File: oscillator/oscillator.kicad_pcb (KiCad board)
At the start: 2 copper layers, 80.5 x 147.8 mm, 37 parts, among them J1 Output, J2 Output, J3 Triangle Output, J4 Saw Output, J5 Pulse Output, J6 Frequency CV Input, J7 PWM CV Input, SW1 LFO Switch, U1 AS3340-custom, U2 TL074

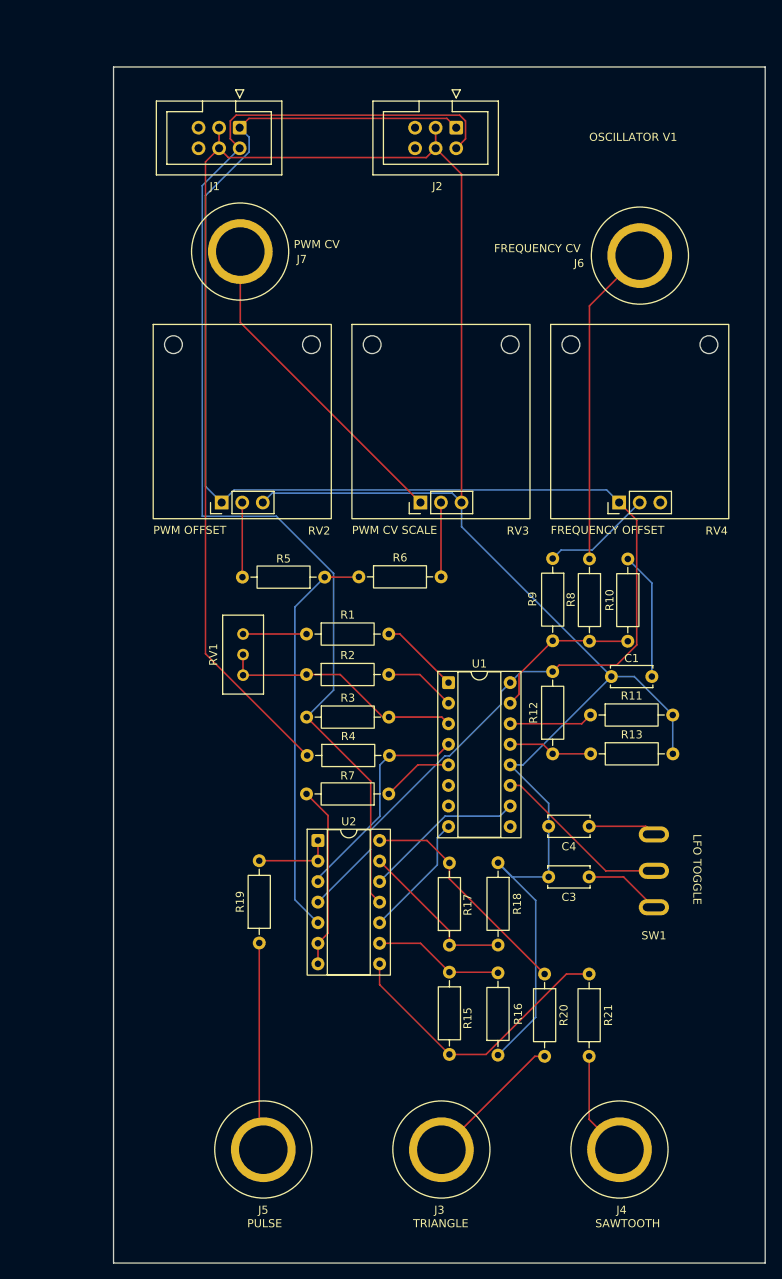
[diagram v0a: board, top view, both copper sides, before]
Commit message: Redesign oscillator
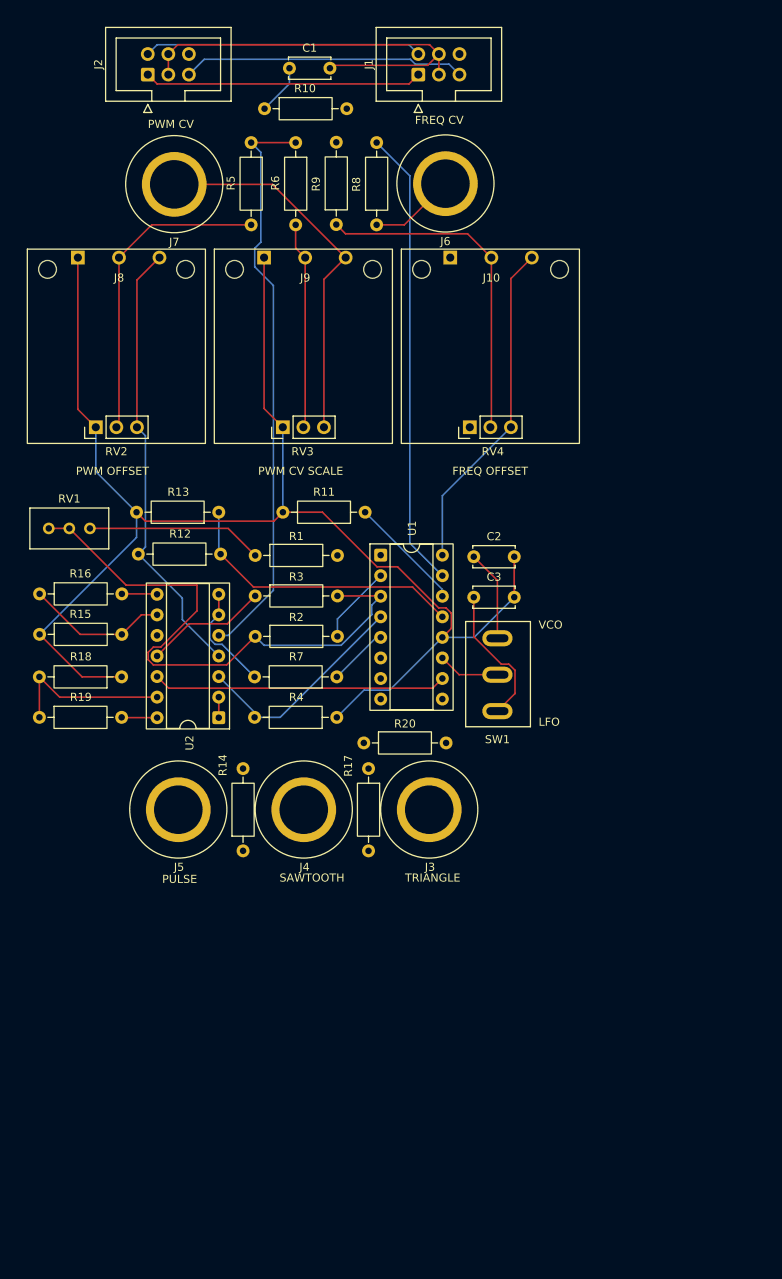
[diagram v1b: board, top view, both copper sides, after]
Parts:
- removed C4: 470nF, Capacitor_THT:C_Disc_D5.0mm_W2.5mm_P5.00mm
- removed R21: 1K, Resistor_THT:R_Axial_DIN0207_L6.3mm_D2.5mm_P10.16mm_Horizontal
- added C2: 4.7nF, Capacitor_THT:C_Disc_D5.0mm_W2.5mm_P5.00mm, F.Cu at (106.0, 92.8)
- added J10: Conn_01x03_Socket, modular2:pot, F.Cu at (108.2, 58.8)
- added J8: Conn_01x03_Socket, modular2:pot, F.Cu at (62.2, 58.8)
- added J9: Conn_01x03_Socket, modular2:pot, F.Cu at (85.2, 58.8)
- added R14: 1K, Resistor_THT:R_Axial_DIN0207_L6.3mm_D2.5mm_P10.16mm_Horizontal, F.Cu at (77.5, 129.1)
- C3: value 4.7nF -> 470nF
- R15: value 24K -> 100K
- R16: value 100K -> 24K
- R17: value 20K -> 1K
- R19: value 1K -> 20K
- moved C1 87.5 mm to (83.2, 32.4), turned to 0 degrees
- moved R16 80.3 mm to (52.4, 97.3), turned to 0 degrees
- moved R10 71.5 mm to (80.2, 37.4), turned to 0 degrees
- moved J4 68.2 mm to (85.0, 124.0)
- moved R15 65.6 mm to (52.4, 102.3), turned to 0 degrees
- moved J5 57.0 mm to (69.5, 124.0)
- moved J3 56.0 mm to (100.5, 124.0)
- moved R13 54.8 mm to (74.5, 87.2), turned to 180 degrees
- moved R5 54.4 mm to (78.5, 41.6), turned to -90 degrees
- moved R6 54.2 mm to (84.0, 41.6), turned to -90 degrees
- moved R18 51.9 mm to (62.5, 107.6), turned to 180 degrees
- moved R9 49.2 mm to (89.0, 51.7), turned to 90 degrees
- moved R8 48.9 mm to (94.0, 51.8), turned to 90 degrees
- moved R12 47.9 mm to (74.7, 92.4), turned to 180 degrees
- moved R19 38.9 mm to (52.3, 112.6), turned to 0 degrees
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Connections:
- C3 pad 1: Net-(SW1-A) -> Net-(SW1-C)
- J1 pad 5: unconnected-(J1-Pin_5-Pad5) -> 5V
- J2 pad 5: unconnected-(J2-Pin_5-Pad5) -> 5V
- R15 pad 1: Net-(U2C--) -> GND
- R15 pad 2: Net-(R15-Pad2) -> Net-(U2C--)
- R16 pad 1: GND -> Net-(U2C--)
- R16 pad 2: Net-(U2C--) -> Net-(R16-Pad2)
- R17 pad 1: Net-(U2D--) -> Net-(R16-Pad2)
- R17 pad 2: Net-(R17-Pad2) -> Net-(J4-Pin_1)
- R19 pad 1: Net-(J5-Pin_1) -> Net-(U2D--)
- R19 pad 2: Net-(U2A--) -> Net-(R19-Pad2)
- R20 pad 1: Net-(R17-Pad2) -> Net-(R19-Pad2)
- RV2 pad 1: 12V -> GND
- RV2 pad 3: GND -> 12V
- RV3 pad 1: Net-(J7-Pin_1) -> GND
- RV3 pad 3: GND -> Net-(J7-Pin_1)
- RV4 pad 1: 12V -> unconnected-(RV4-Pad1)
- RV4 pad 3: unconnected-(RV4-Pad3) -> 12V
- U2 pad 14: Net-(R17-Pad2) -> Net-(R19-Pad2)
- U2 pad 8: Net-(R15-Pad2) -> Net-(R16-Pad2)
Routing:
- net -12V: track 149.6 -> 49.6 mm
- net 12V: track 201.3 -> 131.0 mm
- net GND: track 295.2 -> 234.3 mm
- net Net-(U1-VEE): track 30.5 -> 72.9 mm
- net Net-(U1-VFCI): track 19.2 -> 56.9 mm
- net Net-(R15-Pad2): track 36.1 -> 0.00 mm
- net 5V: track 0.00 -> 35.0 mm
- net Net-(J8-Pin_2): track 9.23 -> 39.1 mm
- net Net-(J5-Pin_1): track 29.6 -> 0.00 mm
- net Net-(J6-Pin_1): track 40.0 -> 10.6 mm
- net Net-(R17-Pad2): track 28.4 -> 0.00 mm
- net Net-(J10-Pin_2): track 13.6 -> 41.9 mm
- net Net-(U1-VLFI): track 10.4 -> 35.9 mm
- net Net-(U2B-+): track 49.6 -> 71.6 mm
- net Net-(J3-Pin_1): track 18.6 -> 0.00 mm
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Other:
- board outline removed
- board text added: "FREQ CV"
- board text added: "FREQ OFFSET"
- board text added: "LFO"
- board text added: "VCO"
- board text removed: "FREQUENCY CV"
- board text removed: "FREQUENCY OFFSET"
- board text removed: "LFO TOGGLE"
- board text removed: "OSCILLATOR V1"

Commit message: V2 of oscillator
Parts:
- moved R11 3.44 mm to (89.1, 87.3)
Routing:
- net -12V: track 49.6 -> 122.0 mm
- net 12V: track 131.0 -> 183.5 mm
- net Net-(R16-Pad2): track 4.94 -> 50.7 mm
- net Net-(U1-VSO): track 0.00 -> 34.6 mm
- net Net-(R19-Pad2): track 4.40 -> 31.2 mm
- net GND: track 234.3 -> 260.5 mm
- net Net-(J5-Pin_1): track 0.00 -> 10.1 mm
- net Net-(J4-Pin_1): track 0.00 -> 10.1 mm
- net Net-(J3-Pin_1): track 0.00 -> 9.11 mm
- net Net-(U1-VFCI): track 56.9 -> 65.8 mm
- net Net-(U2A--): track 2.54 -> 10.1 mm
- net Net-(U1-SCALE1): track 0.00 -> 5.36 mm
- net Net-(U1-VS): track 14.3 -> 17.3 mm
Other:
- board outline added: 69 x 108 mm
- board text added: "OSCILLATOR V2"

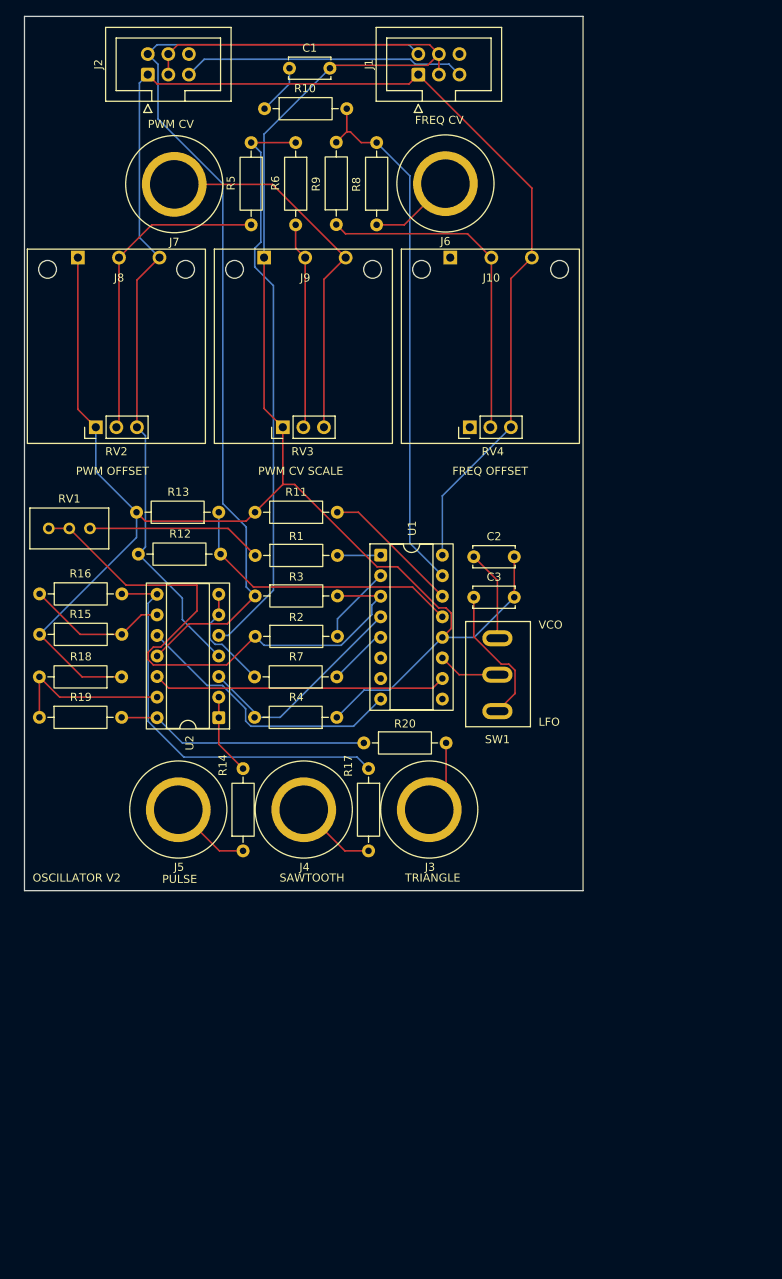
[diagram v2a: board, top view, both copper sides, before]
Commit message: Update oscillator
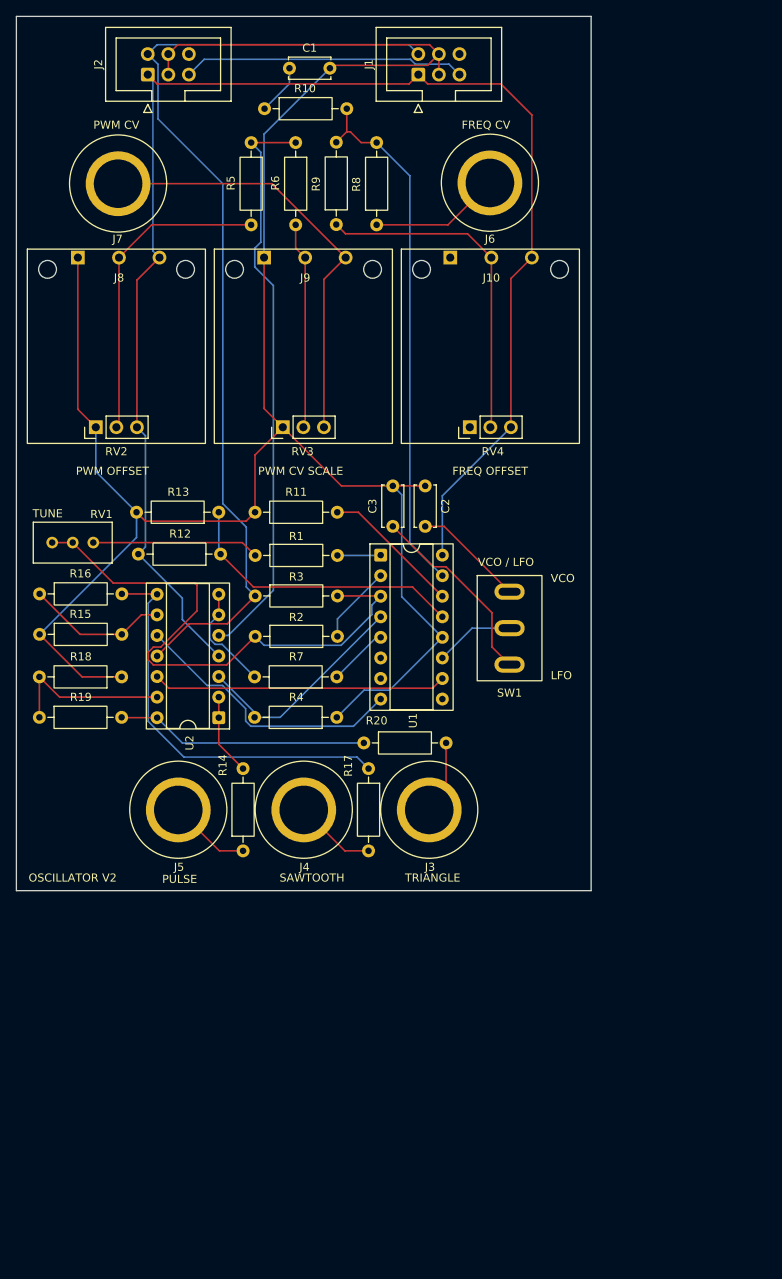
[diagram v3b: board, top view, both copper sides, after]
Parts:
- added F1: foot, modular2:foot, B.Cu at (56.5, 33.0)
- added F2: foot, modular2:foot, B.Cu at (113.5, 33.0)
- added F3: foot, modular2:foot, B.Cu at (56.5, 126.5)
- added F4: foot, modular2:foot, B.Cu at (113.5, 126.5)
- moved J7 15.7 mm to (62.1, 46.6)
- moved J6 15.1 mm to (108.0, 46.5)
- moved C3 13.3 mm to (96.0, 89.0), turned to 90 degrees
- moved C2 7.08 mm to (100.0, 89.0), turned to 90 degrees
- moved SW1 5.94 mm to (110.4, 110.1)
- moved RV1 1.80 mm to (59.0, 91.0)
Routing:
- net Net-(J7-Pin_1): track 47.0 -> 54.0 mm
- net Net-(SW1-C): track 17.6 -> 24.0 mm
- net Net-(J6-Pin_1): track 10.6 -> 16.1 mm
- net GND: track 260.5 -> 255.6 mm
- net 12V: track 183.5 -> 187.9 mm
- net Net-(SW1-A): track 11.3 -> 13.8 mm
- net Net-(SW1-B): track 7.66 -> 9.83 mm
- net Net-(U1-VEE): track 72.9 -> 71.8 mm
- net Net-(R1-Pad1): track 21.8 -> 20.7 mm
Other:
- board size 69 x 108 mm -> 71 x 108 mm
- board text added: "TUNE"
- board text added: "VCO / LFO"

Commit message: Add mixer and power expander
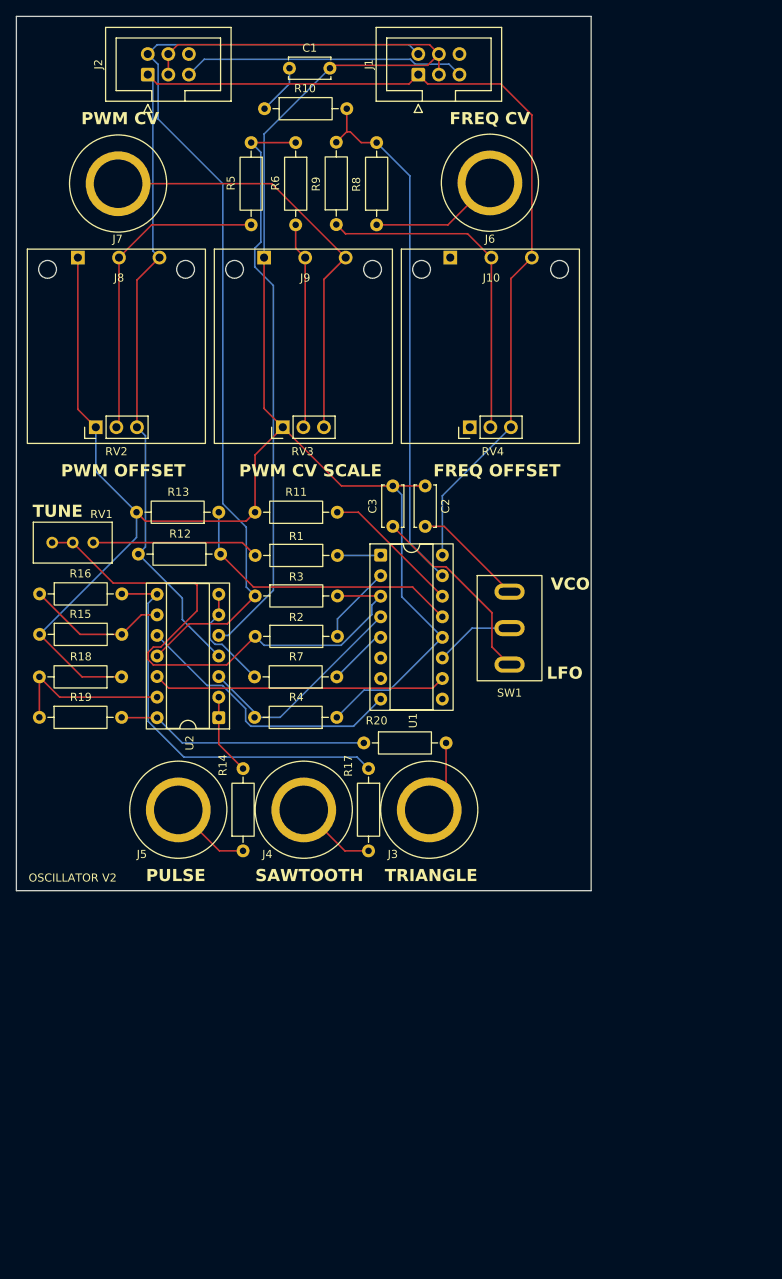
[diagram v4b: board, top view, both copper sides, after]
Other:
- board text removed: "VCO / LFO"
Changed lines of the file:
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@@
 		)
 		(property "Value" "Frequency CV Input"
-			(at -1.269 -22.721469 0)
+			(at 4.004324 -5.548247 0)
 			(unlocked yes)
 			(layer "F.Fab")
@@
 		)
 		(fp_text user "${REFERENCE}"
-			(at -0.769 -21.221469 0)
+			(at 4.504324 -4.048247 0)
 			(unlocked yes)
 			(layer "F.Fab")
@@
 		)
 		(property "Value" "PWM CV Input"
-			(at -1.269 -22.721469 0)
+			(at -6.563928 -5.644742 0)
 			(unlocked yes)
 			(layer "F.Fab")
@@
 		)
 		(fp_text user "${REFERENCE}"
-			(at -0.769 -21.221469 0)
+			(at -6.063928 -4.144742 0)
 			(unlocked yes)
 			(layer "F.Fab")
@@
 		(at 100.5 124)
 		(property "Reference" "J3"
-			(at 0.09 7.087531 0)
+			(at -4.5 5.5 0)
 			(unlocked yes)
 			(layer "F.SilkS")
@@
 		(at 85 124)
 		(property "Reference" "J4"
-			(at 0.09 7.087531 0)
+			(at -4.5 5.5 0)
 			(unlocked yes)
 			(layer "F.SilkS")
@@
 		(at 69.5 124)
 		(property "Reference" "J5"
-			(at 0.09 7.087531 0)
+			(at -4.5 5.5 0)
 			(unlocked yes)
 			(layer "F.SilkS")
@@
 	)
 	(gr_text "PWM OFFSET"
-		(at 56.85 82.75 0)
+		(at 55 83 0)
 		(layer "F.SilkS")
 		(effects
 			(font
-				(size 1 1)
-				(thickness 0.1)
+				(size 1.5 1.5)
+				(thickness 0.3)
+				(bold yes)
 			)
 			(justify left bottom)
@@
 	)
 	(gr_text "SAWTOOTH"
-		(at 82 133 0)
+		(at 79 133 0)
 		(layer "F.SilkS")
 		(effects
 			(font
-				(size 1 1)
-				(thickness 0.1)
+				(size 1.5 1.5)
+				(thickness 0.3)
+				(bold yes)
 			)
 			(justify left bottom)
@@
 	)
 	(gr_text "FREQ OFFSET"
-		(at 103.35 82.75 0)
+		(at 101 83 0)
 		(layer "F.SilkS")
 		(effects
 			(font
-				(size 1 1)
-				(thickness 0.1)
+				(size 1.5 1.5)
+				(thickness 0.3)
+				(bold yes)
 			)
 			(justify left bottom)
@@
 	)
 	(gr_text "PWM CV SCALE"
-		(at 79.35 82.75 0)
+		(at 77 83 0)
 		(layer "F.SilkS")
 		(effects
 			(font
-				(size 1 1)
-				(thickness 0.1)
+				(size 1.5 1.5)
+				(thickness 0.3)
+				(bold yes)
 			)
 			(justify left bottom)
@@
 	)
 	(gr_text "LFO"
-		(at 115.5 108 0)
+		(at 115 108 0)
 		(layer "F.SilkS")
 		(effects
 			(font
-				(size 1 1)
-				(thickness 0.1)
+				(size 1.5 1.5)
+				(thickness 0.3)
+				(bold yes)
 			)
 			(justify left bottom)
@@
 		(effects
 			(font
-				(size 1 1)
-				(thickness 0.1)
+				(size 1.5 1.5)
+				(thickness 0.3)
+				(bold yes)
 			)
 			(justify left bottom)
@@
 	)
 	(gr_text "VCO"
-		(at 115.5 96 0)
+		(at 115.5 97 0)
 		(layer "F.SilkS")
 		(effects
 			(font
-				(size 1 1)
-				(thickness 0.1)
+				(size 1.5 1.5)
+				(thickness 0.3)
+				(bold yes)
 			)
 			(justify left bottom)
@@
 	)
 	(gr_text "FREQ CV"
-		(at 104.5 40 0)
+		(at 103 39.5 0)
 		(layer "F.SilkS")
 		(effects
 			(font
-				(size 1 1)
-				(thickness 0.1)
-			)
-			(justify left bottom)
-		)
-	)
-	(gr_text "VCO / LFO"
-		(at 106.5 94 0)
-		(layer "F.SilkS")
-		(effects
-			(font
-				(size 1 1)
-				(thickness 0.1)
+				(size 1.5 1.5)
+				(thickness 0.3)
+				(bold yes)
 			)
 			(justify left bottom)
@@
 	)
 	(gr_text "PWM CV"
-		(at 59 40 0)
+		(at 57.5 39.5 0)
 		(layer "F.SilkS")
 		(effects
 			(font
-				(size 1 1)
-				(thickness 0.1)
+				(size 1.5 1.5)
+				(thickness 0.3)
+				(bold yes)
 			)
 			(justify left bottom)
@@
 	)
 	(gr_text "TRIANGLE"
-		(at 97.5 133 0)
+		(at 95 133 0)
 		(layer "F.SilkS")
 		(effects
 			(font
-				(size 1 1)
-				(thickness 0.1)
+				(size 1.5 1.5)
+				(thickness 0.3)
+				(bold yes)
 			)
 			(justify left bottom)
@@
 	)
 	(gr_text "PULSE"
-		(at 67.5 133.162469 0)
+		(at 65.5 133 0)
 		(layer "F.SilkS")
 		(effects
 			(font
-				(size 1 1)
-				(thickness 0.1)
+				(size 1.5 1.5)
+				(thickness 0.3)
+				(bold yes)
 			)
 			(justify left bottom)

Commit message: More space for backup pot
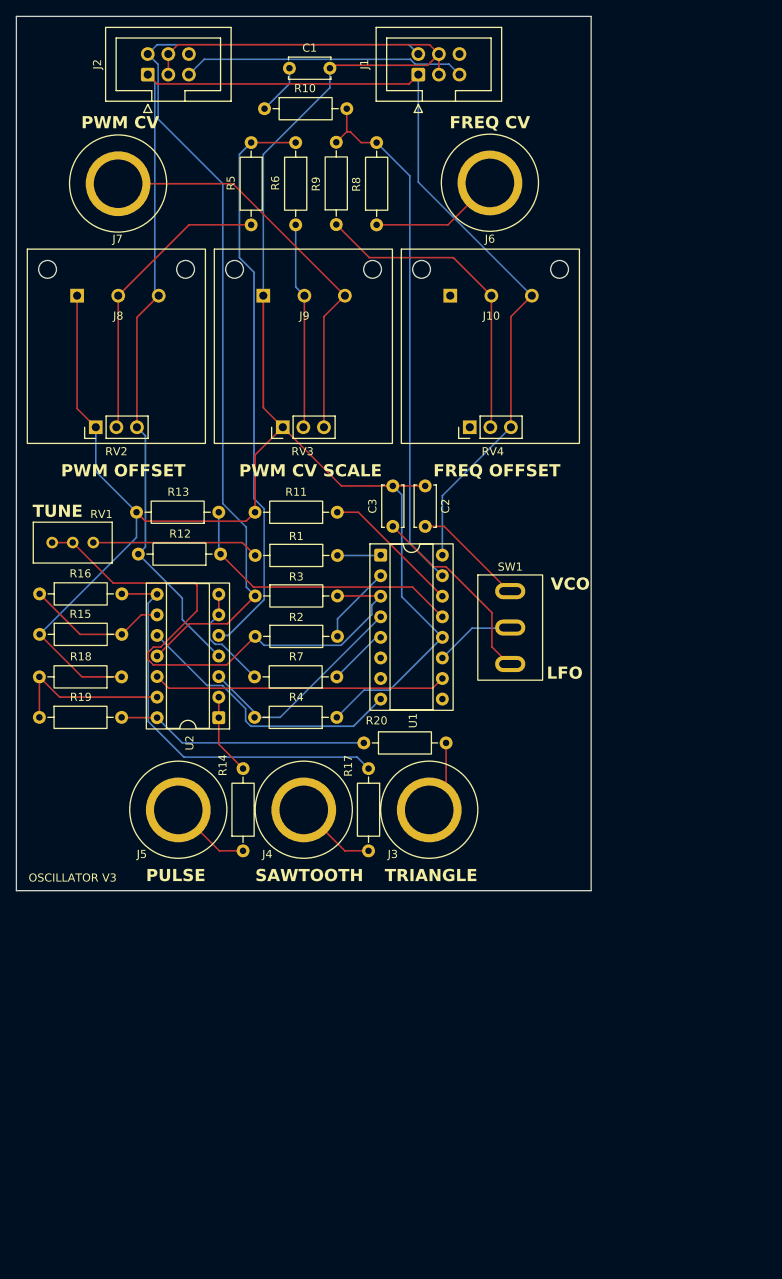
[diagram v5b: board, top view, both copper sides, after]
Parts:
- moved SW1 8.57 mm to (110.5, 101.5)
- moved J8 4.71 mm to (62.1, 63.5)
- moved J9 4.71 mm to (85.1, 63.5)
- moved J10 4.70 mm to (108.2, 63.5)
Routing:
- net 12V: track 187.9 -> 182.5 mm
- net GND: track 255.6 -> 251.2 mm
- net Net-(J7-Pin_1): track 54.0 -> 51.1 mm
- net Net-(J10-Pin_2): track 41.9 -> 39.1 mm
- net Net-(J8-Pin_2): track 39.1 -> 36.8 mm
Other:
- board text added: "OSCILLATOR V3"
- board text removed: "OSCILLATOR V2"

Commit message: Various improvements
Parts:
- added C4: 100nf, Capacitor_THT:C_Disc_D4.3mm_W1.9mm_P5.00mm, F.Cu at (64.0, 110.0)
- added C5: 100nf, Capacitor_THT:C_Disc_D4.3mm_W1.9mm_P5.00mm, F.Cu at (77.5, 106.0)
- added C6: 100nf, Capacitor_THT:C_Disc_D4.3mm_W1.9mm_P5.00mm, F.Cu at (105.0, 93.5)
- added G***: LOGO, modular2:ibis-small, F.Cu at (116.5, 129.0)
- J1, J2: value Output -> Power
- moved R18 9.18 mm to (59.0, 116.1), turned to 90 degrees
- moved R19 6.67 mm to (52.4, 105.9), turned to -90 degrees
- moved R7 1.91 mm to (89.1, 109.5)
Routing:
- net GND: track 251.2 -> 274.8 mm
- net Net-(R19-Pad2): track 31.2 -> 42.8 mm
- net 12V: track 182.5 -> 189.2 mm
- net Net-(U2D--): track 20.6 -> 16.2 mm
- net Net-(U1-VTO): track 36.3 -> 40.4 mm
- net Net-(U2B--): track 13.4 -> 17.5 mm
- net -12V: track 122.0 -> 124.8 mm
- net Net-(R16-Pad2): track 50.7 -> 52.6 mm
- net Net-(U1-VPWM): track 7.98 -> 9.04 mm
